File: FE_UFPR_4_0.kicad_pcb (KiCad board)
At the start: 4 copper layers, 146 x 130 mm, 379 parts, among them J1 Mini-Fit Jr 5566-02A, J2 DSUB-37_Socket, J20 LaunchPad J1+J3, J21 LaunchPad J4+J2, J22 LaunchPad J5+J7, J23 LaunchPad J8+J6, J3 LEM DTM13-12PA-R005 key A, J4 ENC DTM13-12PB-R005 key B, J5 VEH DTM13-08PA-R004 key A, Q1 SQD50P06-15L, U1 LMR33630ADDAR, U10 SN74LVC2G17DBVR, U11 SN74LVC2G17DBVR, U12 OPA2376, U13 OPA2376, U14 OPA2376, U15 OPA2376, U16 OPA2376, U17 OPA2376, U18 SN65HVD230DR, U19 LTV-817S-TA1-C, U2 TPS62933FDRLR, U20 LTV-817S-TA1-C, U21 SN74LVC2G17DBVR, U3 AMS1117-3.3, U4 URA2415YMD-6WR3, U5 UCC27524DR, U6 UCC27524DR, U7 UCC27524DR, U8 SN74LVC1G11DBVR, U9 SN74LVC2G17DBVR

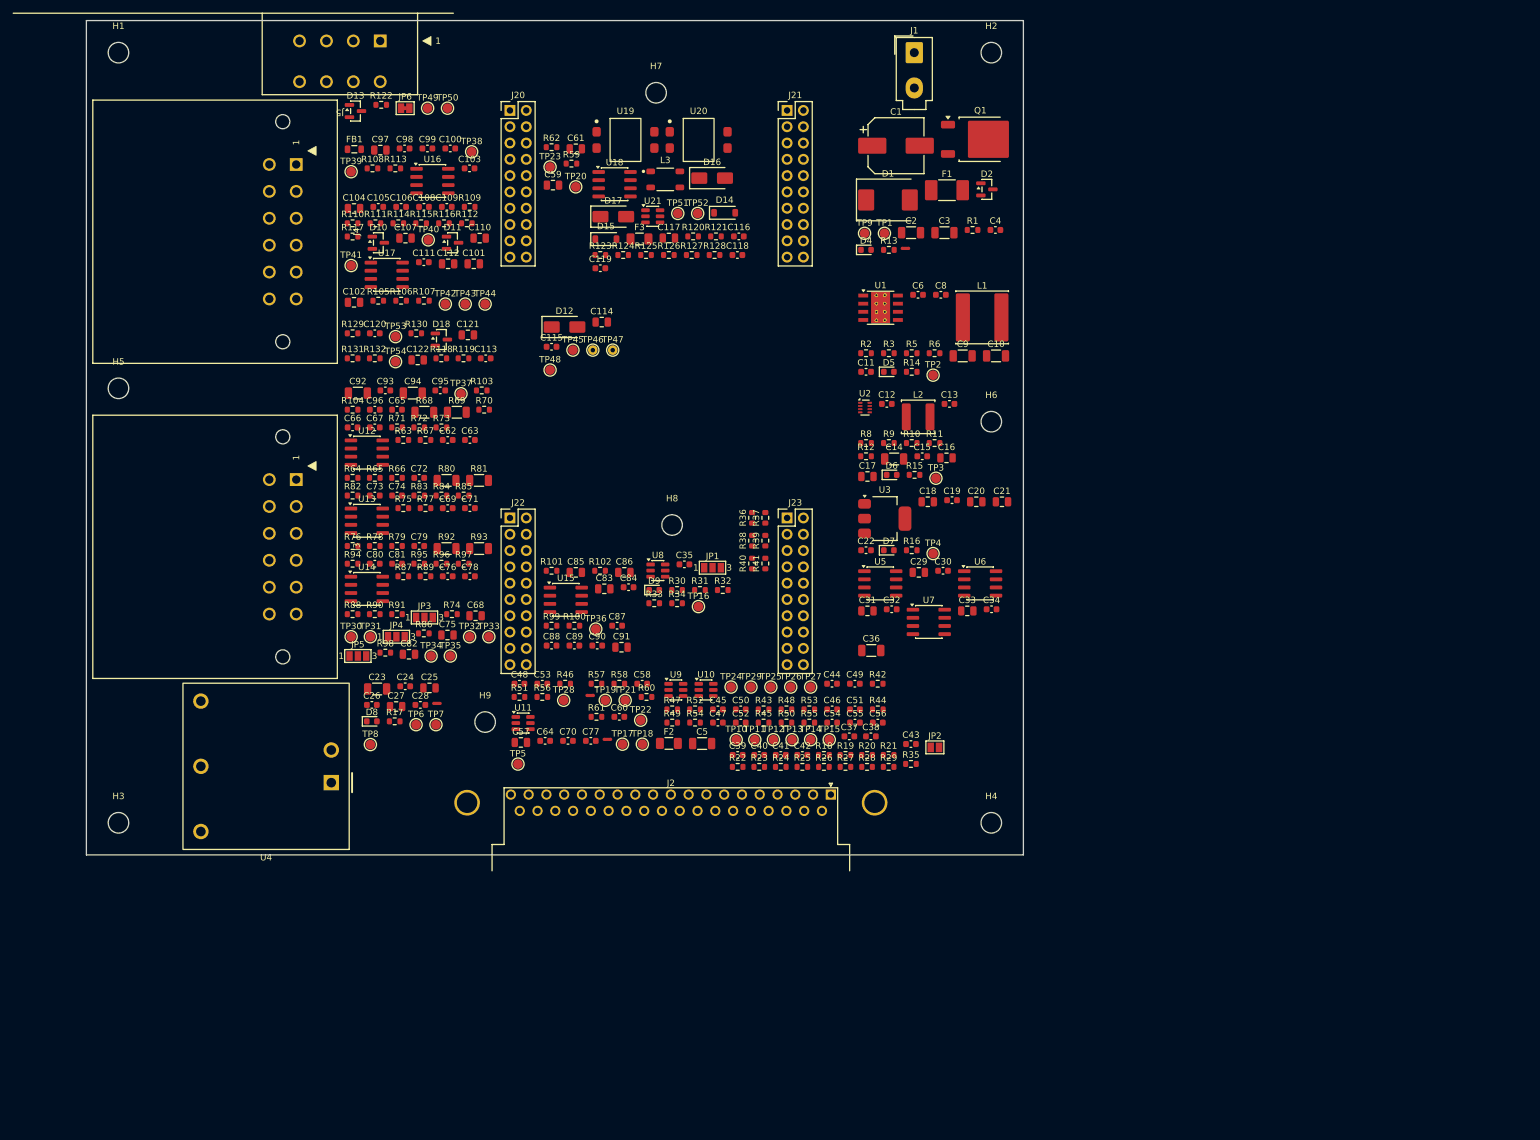
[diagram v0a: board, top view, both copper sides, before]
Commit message: Placing power segment components
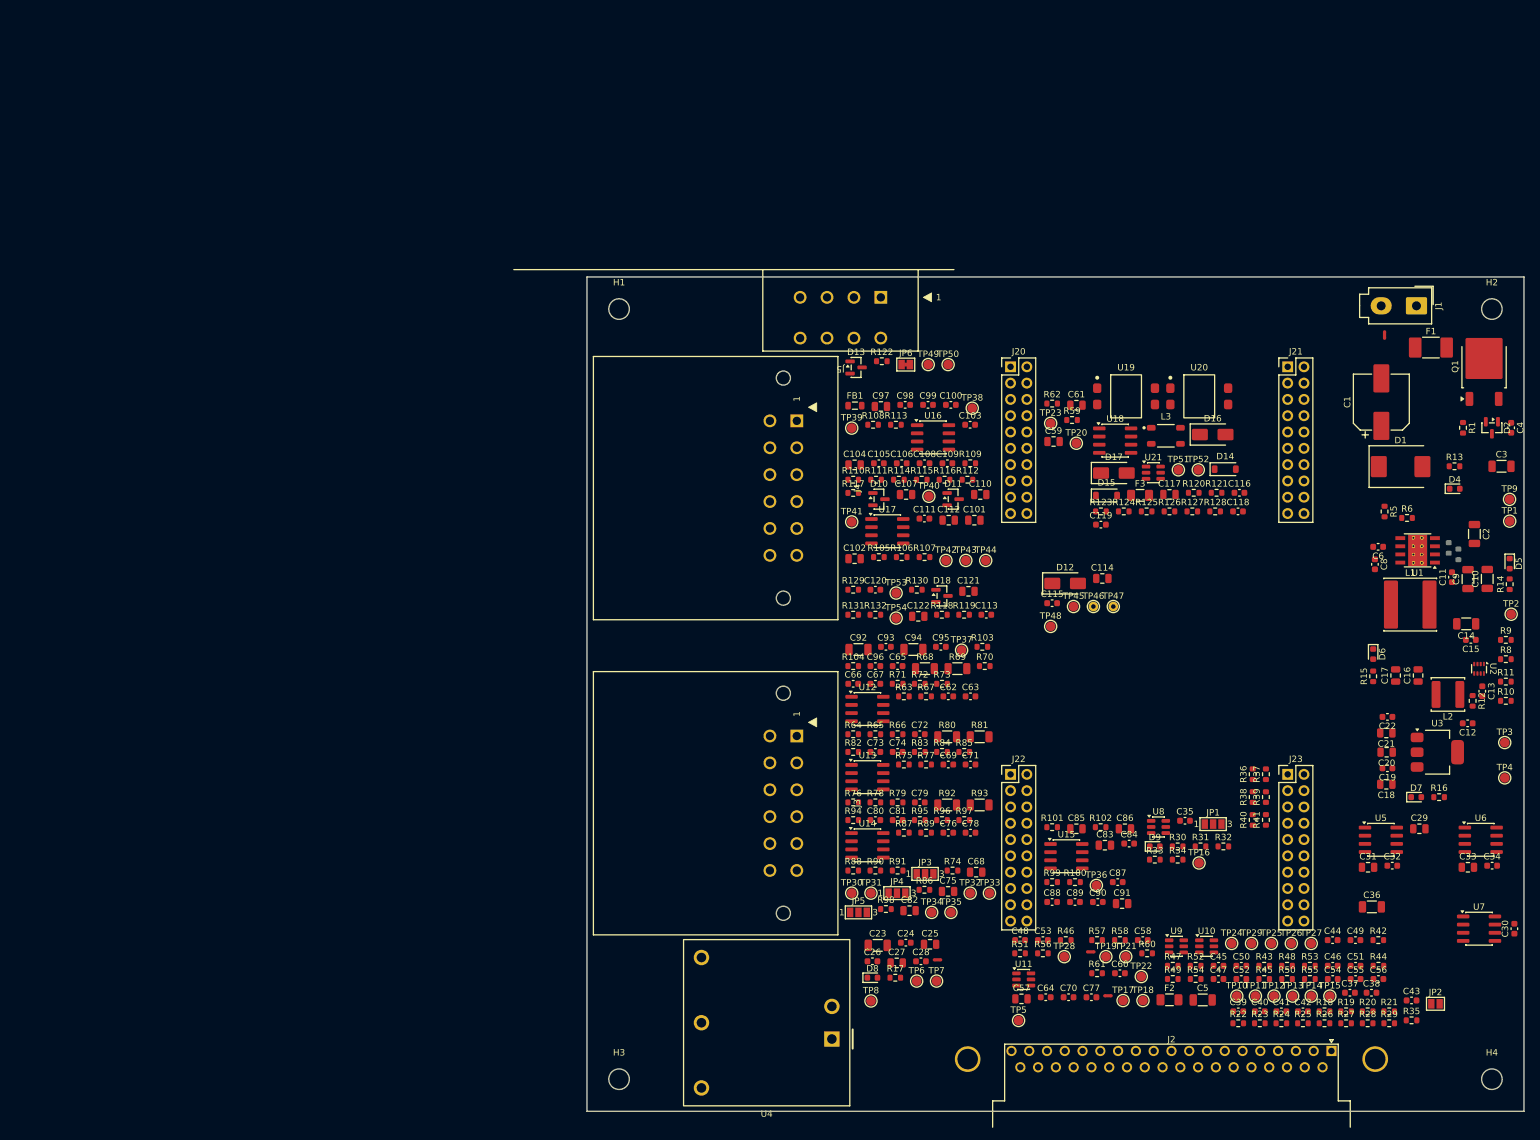
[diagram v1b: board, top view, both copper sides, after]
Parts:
- removed H5, H6: M3 board mount, FE_UFPR_4_0:MountingHole_3.2mm_M3
- removed H7, H8, H9: M3 LaunchPad standoff, FE_UFPR_4_0:MountingHole_3.2mm_M3
- R2, R3: moved to B.Cu
- moved TP9 108.7 mm to (271.8, 124.6)
- moved TP1 107.3 mm to (271.8, 128.0)
- moved R8 105.2 mm to (271.2, 149.5)
- moved C30 105.0 mm to (272.5, 191.5), turned to 90 degrees
- moved U2 104.0 mm to (267.0, 151.0), turned to -90 degrees
- moved C12 103.3 mm to (265.2, 159.5), turned to 180 degrees
- moved R12 101.9 mm to (266.0, 156.0), turned to -90 degrees
- moved D5 101.2 mm to (271.8, 134.6), turned to -90 degrees
- moved R10 100.9 mm to (271.2, 156.0)
- moved R9 100.9 mm to (271.2, 146.5)
- moved C2 99.5 mm to (266.3, 130.0), turned to -90 degrees
- moved D4 99.0 mm to (263.2, 123.0)
- moved R14 98.9 mm to (271.8, 137.8), turned to 90 degrees
- moved U7 98.2 mm to (267.0, 191.5)
- moved TP3 97.7 mm to (271.0, 162.5)
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
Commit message: pwm placement
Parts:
- moved TP28 111.7 mm to (309.0, 229.0)
- moved NT3 98.1 mm to (304.5, 197.8)
- moved TP21 98.1 mm to (310.0, 198.5)
- moved TP22 98.1 mm to (312.4, 201.6)
- moved C58 98.1 mm to (312.6, 195.9)
- moved C60 98.1 mm to (309.1, 201.1)
- moved R57 98.1 mm to (305.5, 195.9)
- moved R58 98.1 mm to (309.1, 195.9)
- moved R60 98.1 mm to (313.3, 198.0)
- moved R61 98.1 mm to (305.5, 201.1)
- moved TP19 98.1 mm to (306.9, 198.5)
- moved TP36 78.6 mm to (165.7, 251.4)
- moved C83 78.6 mm to (167.0, 245.1)
- moved C84 78.6 mm to (170.8, 244.9)
- moved C85 78.6 mm to (162.6, 242.6)
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
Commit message: POwer interface fixes
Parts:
- moved D16 45.2 mm to (230.2, 69.5)
- moved U19 31.5 mm to (222.9, 79.0)
- moved U20 31.5 mm to (234.3, 79.0)
- moved D13 28.0 mm to (197.6, 99.7), turned to -90 degrees
- moved U18 21.3 mm to (231.6, 115.6), turned to 180 degrees
- moved L3 20.9 mm to (204.1, 99.2)
